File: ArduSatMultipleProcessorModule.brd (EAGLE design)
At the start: 95.5 x 90.3 mm, 82 parts, among them IC1 ATMEGA328P, IC2 ATMEGA328P, IC3 ATMEGA328P, IC4 ATMEGA328P, IC5 MCP23017SO, IC6 MCP23017SO, P1 N1_ICSP, P2 N0_ICSP, P3 N0_ICSP, P4 N1_ICSP, Q1 BSS138 N-MOSFET, Q2 BSS138 N-MOSFET, Q3 BSS138 N-MOSFET, Q4 BSS138 N-MOSFET, Q5 BSS138 N-MOSFET, Q6 BSS138 N-MOSFET, Q7 BSS138 N-MOSFET, Q8 BSS138 N-MOSFET, U1 MUX-74HC4067, U2 MUX-74HC4067

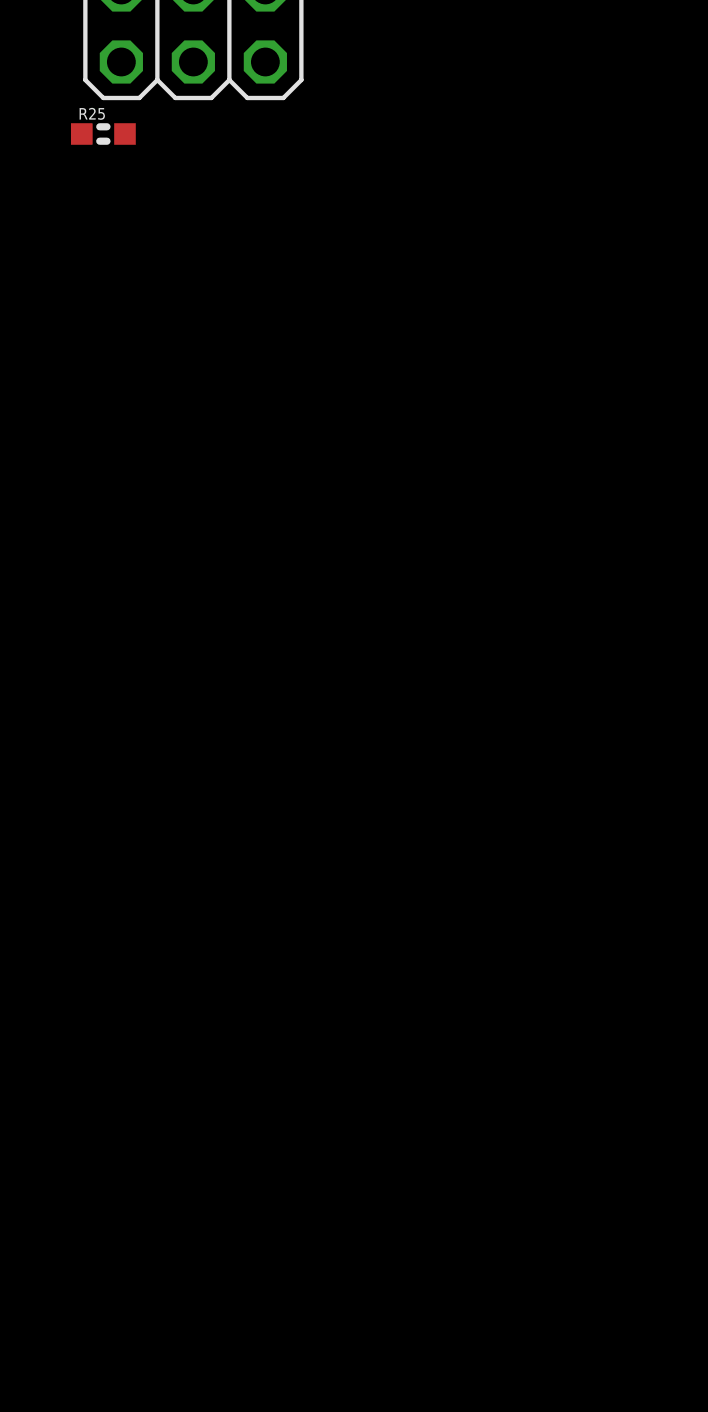
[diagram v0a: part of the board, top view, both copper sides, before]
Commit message: Testing replacement of latches using ATmega328
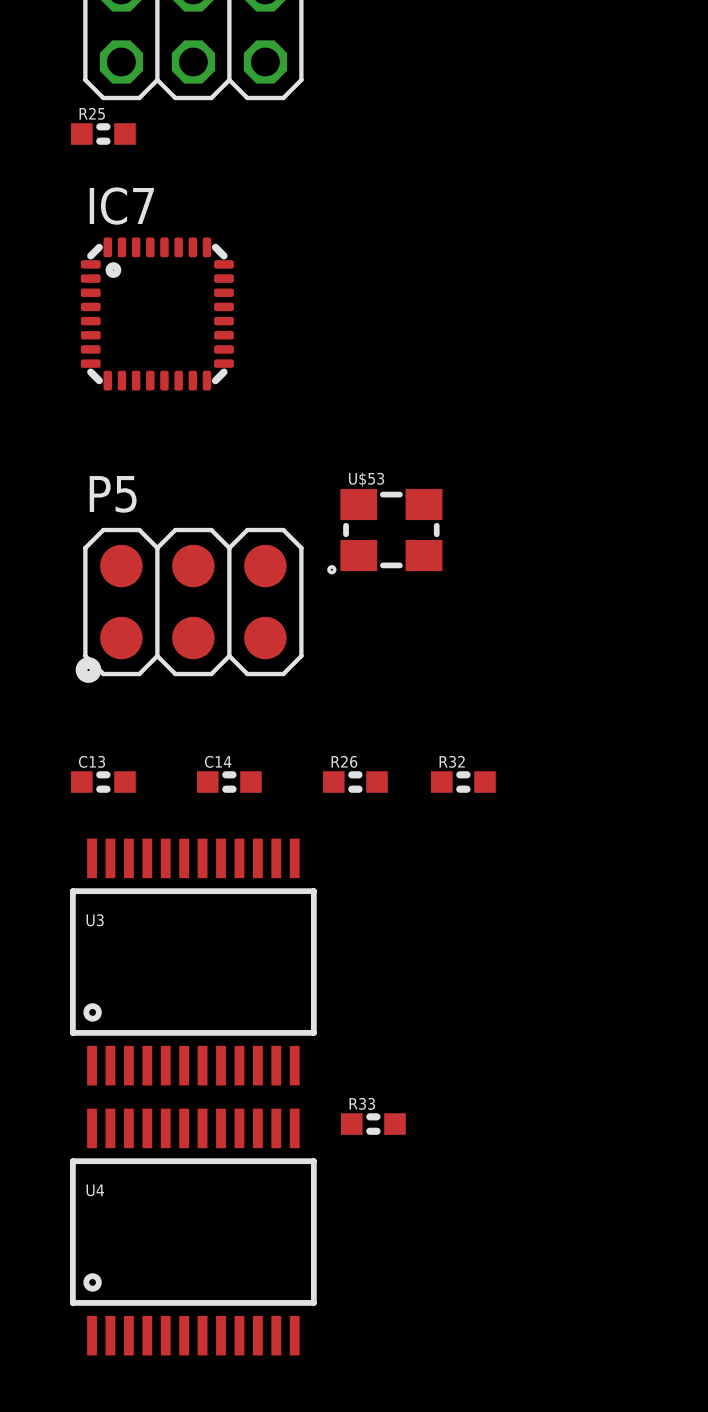
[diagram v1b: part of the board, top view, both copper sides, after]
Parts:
- added C13, C14: 22pF 0603, freetronics-master-v1.1:0603
- added IC7: ATMEGA328P, freetronics-master-v1.1:MLF32
- added P5: N1_ICSP, freetronics-jon:2X03SURFACE
- added R26: 22K 0603, freetronics-master-v1.1:0603
- added R32: 1M 0603, freetronics-master-v1.1:0603
- added R33: 33K 0603, freetronics-master-v1.1:0603
- added U$53: CRYSTAL-GND3X2, freetronics-jon:CRYSTAL-SMD-3X2
- added U3, U4: MUX-74HC4067, SparkFun:SSOP24
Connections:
- removed net MGMNT_SCL: IC5.12, IC6.12, R25.1, R27.1
- removed net MGMNT_SDA: IC5.13, IC6.13, R24.1, R28.1
- removed net S0: IC5.21, U1.10, U2.10
- removed net S1: IC5.22, U1.11, U2.11
- removed net S2: IC5.23, U1.14, U2.14
- removed net S3: IC5.24, U1.13, U2.13
- new net N$22: C14.2, IC7.8, R32.1, U$53.3
- new net N$23: C13.2, IC7.7, R32.2, U$53.1
- new net S_A0: IC5.21, IC7.23, U1.10, U2.10, U3.10, U4.10
- new net S_A1: IC5.22, IC7.24, U1.11, U2.11, U3.11, U4.11
- new net S_A2: IC5.23, IC7.25, U1.14, U2.14, U3.14, U4.14
- new net S_A3: IC5.24, IC7.26, U1.13, U2.13, U3.13, U4.13
- new net S_A4_SDA: IC5.13, IC6.13, IC7.27, R24.1, R28.1
- new net S_A5_SCL: IC5.12, IC6.12, IC7.28, R25.1, R27.1
- new net S_A6: IC7.19
- new net S_A7: IC7.22
- new net S_D0_RX: IC7.30
- new net S_D10: IC7.14
- new net S_D11_MOSI: IC7.15, P5.4
- new net S_D12_MISO: IC7.16, P5.1
- new net S_D13_SCK: IC7.17, P5.3
- new net S_D1_TX: IC7.31
- new net S_D2: IC7.32
- new net S_D3: IC7.1
- new net S_D4: IC7.2
- new net S_D5: IC7.9
- new net S_D6: IC7.10
- new net S_D7: IC7.11
- new net S_D8: IC7.12
- new net S_D9: IC7.13
- new net S_RESET: IC7.29, P5.5, R26.1
- net +5V_SYS: now also IC7.18, IC7.20, IC7.4, IC7.6, P5.2, R26.2, U3.24, U4.24
- net EN: now also R33.2, U3.15, U4.15
- net GND: now also C13.1, C14.1, IC7.21, IC7.3, IC7.5, P5.6, R33.1, U$53.2, U$53.4, U3.12, U4.12
- net N0_D0_RX: now also U4.9
- net N0_D1_TX: now also U3.9
- net N10_D0_RX: now also U4.21
- net N10_D1_TX: now also U3.21
- net N11_D0_RX: now also U4.20
- net N11_D1_TX: now also U3.20
- net N12_D0_RX: now also U4.19
- net N12_D1_TX: now also U3.19
- net N13_D0_RX: now also U4.18
- net N13_D1_TX: now also U3.18
- net N14_D0_RX: now also U4.17
- net N14_D1_TX: now also U3.17
- net N15_D0_RX: now also U4.16
- net N15_D1_TX: now also U3.16
- net N1_D0_RX: now also U4.8
- net N1_D1_TX: now also U3.8
- net N2_D0_RX: now also U4.7
- net N2_D1_TX: now also U3.7
- net N3_D0_RX: now also U4.6
- net N3_D1_TX: now also U3.6
- net N4_D0_RX: now also U4.5
- net N4_D1_TX: now also U3.5
- net N5_D0_RX: now also U4.4
- net N5_D1_TX: now also U3.4
- net N6_D0_RX: now also U4.3
- net N6_D1_TX: now also U3.3
- net N7_D0_RX: now also U4.2
- net N7_D1_TX: now also U3.2
- net N8_D0_RX: now also U4.23
- net N8_D1_TX: now also U3.23
- net N9_D0_RX: now also U4.22
- net N9_D1_TX: now also U3.22
- net RX: now also U4.1
- net TX: now also U3.1

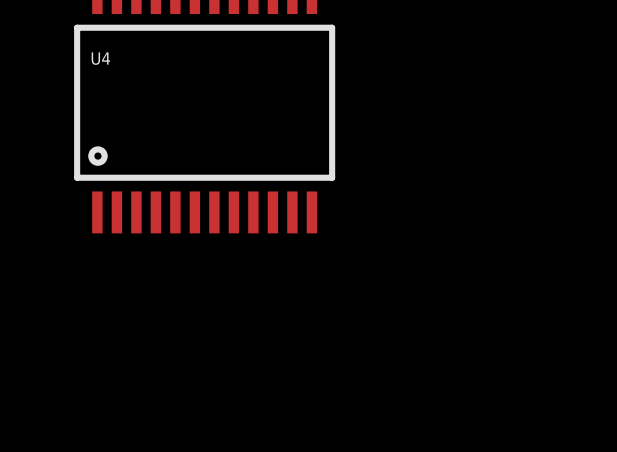
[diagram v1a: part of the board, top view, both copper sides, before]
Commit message: Added alternative supervisor node
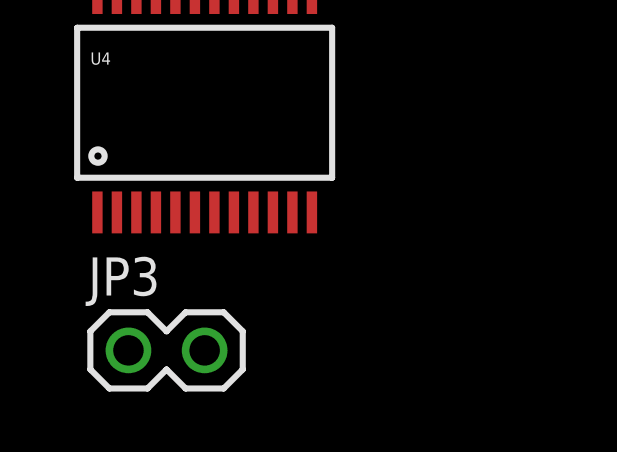
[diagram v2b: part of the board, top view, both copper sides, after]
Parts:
- added JP3: (no value), freetronics-master-v1.1:1X02
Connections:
- net RX: now also JP3.2
- net TX: now also JP3.1
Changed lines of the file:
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@@
 <element name="U4" library="SparkFun" package="SSOP24" value="MUX-74HC4067" x="1.27" y="-220.345"/>
 <element name="R33" library="freetronics-master-v1.1" package="0603" value="33K 0603" x="7.62" y="-216.535"/>
+<element name="JP3" library="freetronics-master-v1.1" package="1X02" value="" x="-1.27" y="-228.6"/>
 </elements>
 <signals>
@@
 <contactref element="U1" pad="1"/>
 <contactref element="U3" pad="1"/>
+<contactref element="JP3" pad="1"/>
+<wire x1="-2.305" y1="-214.476" x2="-1.27" y2="-228.6" width="0" layer="19" extent="1-1"/>
 <wire x1="-2.305" y1="-86.841" x2="-2.305" y2="-214.476" width="0" layer="19" extent="1-1"/>
 </signal>
@@
 <contactref element="U2" pad="1"/>
 <contactref element="U4" pad="1"/>
+<contactref element="JP3" pad="2"/>
+<wire x1="-2.305" y1="-224.001" x2="1.27" y2="-228.6" width="0" layer="19" extent="1-1"/>
 <wire x1="-2.305" y1="-109.701" x2="-2.305" y2="-224.001" width="0" layer="19" extent="1-1"/>
 </signal>

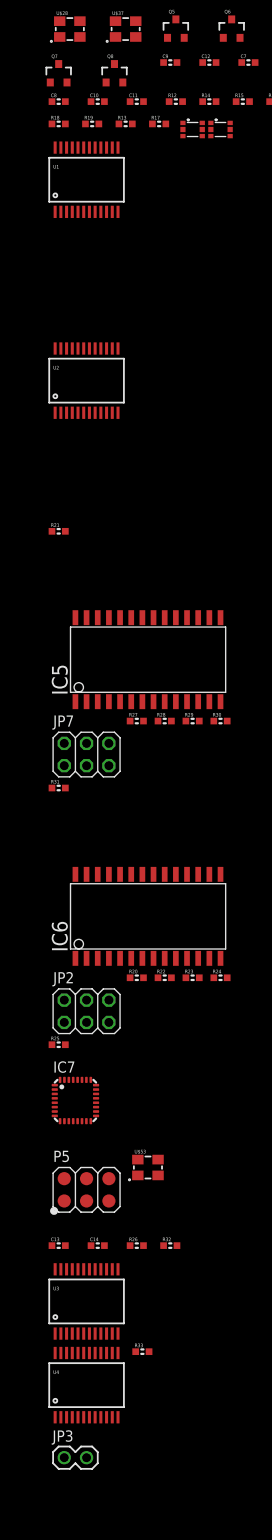
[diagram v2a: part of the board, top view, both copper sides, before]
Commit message: Added VCC control for nodes 0 and 1
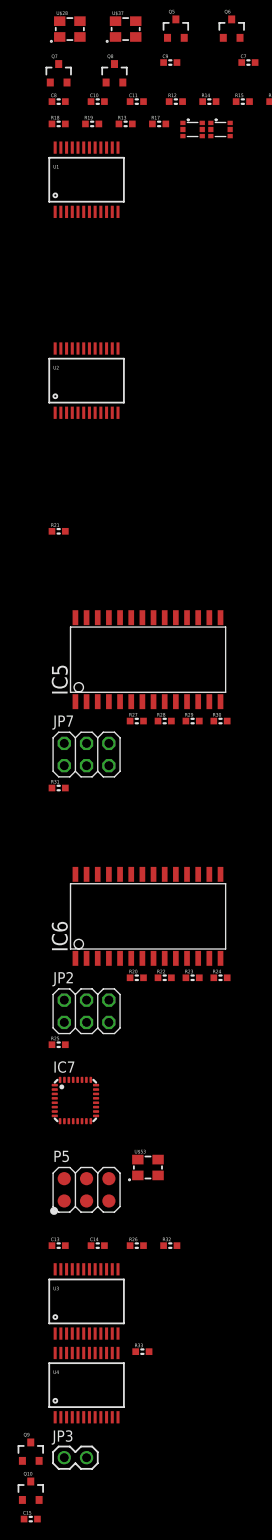
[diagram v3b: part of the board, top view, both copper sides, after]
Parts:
- removed C12: 100nF 0603, freetronics-master-v1.1:0603
- added C15: 100nF 0603, freetronics-master-v1.1:0603
- added Q10, Q9: 2N7002 N-MOSFET, freetronics-master-v1:SOT23-3
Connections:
- net EN renamed UART_EN
- net S_D0_RX renamed S_D0_N2_PWR
- net S_D1_TX renamed S_D1_N3_PWR
- net S_D2 renamed S_D2_N4_PWR
- net S_D3 renamed S_D3_N5_PWR
- net S_D4 renamed S_D4_N6_PWR
- removed net S_A6: IC7.19
- removed net S_A7: IC7.22
- new net S_A6_N0_PWR: IC7.19, Q9.1
- new net S_A7_N1_PWR: IC7.22, Q10.1
- net +5V_SYS: now also Q10.2, Q9.2
- net GND: now also C15.2; no longer C12.2
- net N0_5V: now also Q9.3
- net N1_5V: now also C15.1, Q10.3; no longer C12.1
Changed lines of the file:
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@@
 <element name="C10" library="freetronics-master-v1.1" package="0603" value="22pF 0603" x="2.54" y="-74.295"/>
 <element name="C11" library="freetronics-master-v1.1" package="0603" value="22pF 0603" x="6.985" y="-74.295"/>
-<element name="C12" library="freetronics-master-v1.1" package="0603" value="100nF 0603" x="15.24" y="-69.85"/>
 <element name="R16" library="freetronics-master-v1.1" package="0603" value="22K 0603" x="22.86" y="-74.295"/>
 <element name="P4" library="freetronics-jon" package="2X03SURFACE" value="N1_ICSP" x="10.16" y="-58.42"/>
@@
 <element name="R33" library="freetronics-master-v1.1" package="0603" value="33K 0603" x="7.62" y="-216.535"/>
 <element name="JP3" library="freetronics-master-v1.1" package="1X02" value="" x="-1.27" y="-228.6"/>
+<element name="Q9" library="freetronics-master-v1" package="SOT23-3" value="2N7002 N-MOSFET" x="-5.08" y="-227.965"/>
+<element name="C15" library="freetronics-master-v1.1" package="0603" value="100nF 0603" x="-5.08" y="-235.585"/>
+<element name="Q10" library="freetronics-master-v1" package="SOT23-3" value="2N7002 N-MOSFET" x="-5.08" y="-232.41"/>
 </elements>
 <signals>
@@
 <contactref element="U$37" pad="2"/>
 <contactref element="U$37" pad="4"/>
-<contactref element="C12" pad="2"/>
 <contactref element="IC4" pad="21"/>
 <contactref element="IC4" pad="3"/>
@@
 <contactref element="U3" pad="12"/>
 <contactref element="U4" pad="12"/>
+<contactref element="C15" pad="2"/>
+<wire x1="4.845" y1="-224.001" x2="-4.318" y2="-235.585" width="0" layer="19" extent="1-1"/>
 <wire x1="6.858" y1="-216.535" x2="4.845" y2="-224.001" width="0" layer="19" extent="1-1"/>
 <wire x1="4.845" y1="-214.476" x2="6.858" y2="-216.535" width="0" layer="19" extent="1-1"/>
@@
 <wire x1="-2.667" y1="-74.295" x2="1.778" y2="-74.295" width="0" layer="19" extent="1-1"/>
 <wire x1="11.557" y1="-69.85" x2="6.223" y2="-74.295" width="0" layer="19" extent="1-1"/>
-<wire x1="16.002" y1="-69.85" x2="11.557" y2="-69.85" width="0" layer="19" extent="1-1"/>
-<wire x1="18.923" y1="-69.85" x2="16.002" y2="-69.85" width="0" layer="19" extent="1-1"/>
 <wire x1="6.865" y1="-66.94" x2="11.557" y2="-69.85" width="0" layer="19" extent="1-1"/>
 <wire x1="4.565" y1="-65.14" x2="6.865" y2="-66.94" width="0" layer="19" extent="1-1"/>
 <wire x1="0.515" y1="-66.94" x2="4.565" y2="-65.14" width="0" layer="19" extent="1-1"/>
 <wire x1="-1.785" y1="-65.14" x2="0.515" y2="-66.94" width="0" layer="19" extent="1-1"/>
+<wire x1="18.923" y1="-69.85" x2="11.557" y2="-69.85" width="0" layer="19" extent="1-1"/>
 <wire x1="3.81" y1="-57.15" x2="4.565" y2="-65.14" width="0" layer="19" extent="1-1"/>
 <wire x1="12.7" y1="-57.15" x2="3.81" y2="-57.15" width="0" layer="19" extent="1-1"/>
@@
 <contactref element="IC7" pad="20"/>
 <contactref element="R26" pad="2"/>
+<contactref element="Q9" pad="2"/>
+<contactref element="Q10" pad="2"/>
+<wire x1="-4.13" y1="-228.965" x2="-4.13" y2="-233.41" width="0" layer="19" extent="1-1"/>
+<wire x1="-2.305" y1="-216.689" x2="-4.13" y2="-228.965" width="0" layer="19" extent="1-1"/>
 <wire x1="-2.305" y1="-207.164" x2="-2.305" y2="-216.689" width="0" layer="19" extent="1-1"/>
 <wire x1="-1.27" y1="-196.85" x2="-2.305" y2="-207.164" width="0" layer="19" extent="1-1"/>
@@
 <contactref element="R15" pad="2"/>
 <contactref element="IC6" pad="21"/>
+<contactref element="Q9" pad="3"/>
+<wire x1="8.89" y1="-162.225" x2="-5.08" y2="-226.865" width="0" layer="19" extent="1-1"/>
 <wire x1="14.435" y1="-78.22" x2="8.89" y2="-162.225" width="0" layer="19" extent="1-1"/>
 <wire x1="14.435" y1="-77.47" x2="14.435" y2="-78.22" width="0" layer="19" extent="1-1"/>
@@
 <contactref element="Q7" pad="1"/>
 <contactref element="R18" pad="2"/>
-<contactref element="C12" pad="1"/>
 <contactref element="R16" pad="2"/>
 <contactref element="P4" pad="2"/>
@@
 <contactref element="IC4" pad="20"/>
 <contactref element="IC6" pad="22"/>
+<contactref element="C15" pad="1"/>
+<contactref element="Q10" pad="3"/>
+<wire x1="-5.08" y1="-231.31" x2="-5.842" y2="-235.585" width="0" layer="19" extent="1-1"/>
+<wire x1="7.62" y1="-162.225" x2="-5.08" y2="-231.31" width="0" layer="19" extent="1-1"/>
 <wire x1="17.61" y1="-78.22" x2="7.62" y2="-162.225" width="0" layer="19" extent="1-1"/>
 <wire x1="17.61" y1="-77.47" x2="17.61" y2="-78.22" width="0" layer="19" extent="1-1"/>
 <wire x1="23.622" y1="-74.295" x2="17.61" y2="-77.47" width="0" layer="19" extent="1-1"/>
-<wire x1="14.478" y1="-69.85" x2="17.61" y2="-77.47" width="0" layer="19" extent="1-1"/>
-<wire x1="3.495" y1="-72.12" x2="14.478" y2="-69.85" width="0" layer="19" extent="1-1"/>
-<wire x1="2.667" y1="-76.835" x2="3.495" y2="-72.12" width="0" layer="19" extent="1-1"/>
+<wire x1="2.667" y1="-76.835" x2="17.61" y2="-77.47" width="0" layer="19" extent="1-1"/>
 <wire x1="-1.143" y1="-76.835" x2="2.667" y2="-76.835" width="0" layer="19" extent="1-1"/>
+<wire x1="3.495" y1="-72.12" x2="2.667" y2="-76.835" width="0" layer="19" extent="1-1"/>
 <wire x1="-2.855" y1="-72.12" x2="-1.143" y2="-76.835" width="0" layer="19" extent="1-1"/>
-<wire x1="7.62" y1="-57.15" x2="14.478" y2="-69.85" width="0" layer="19" extent="1-1"/>
+<wire x1="7.62" y1="-57.15" x2="3.495" y2="-72.12" width="0" layer="19" extent="1-1"/>
 <wire x1="10.35" y1="-49.01" x2="7.62" y2="-57.15" width="0" layer="19" extent="1-1"/>
 <wire x1="10.35" y1="-48.01" x2="10.35" y2="-49.01" width="0" layer="19" extent="1-1"/>
@@
 <wire x1="1.25" y1="-20.13" x2="1.27" y2="-26.67" width="0" layer="19" extent="1-1"/>
 </signal>
-<signal name="EN">
+<signal name="UART_EN">
 <contactref element="U1" pad="15"/>
 <contactref element="U2" pad="15"/>
@@
 <contactref element="IC6" pad="8"/>
 </signal>
-<signal name="S_A6">
+<signal name="S_A6_N0_PWR">
 <contactref element="IC7" pad="19"/>
-</signal>
-<signal name="S_A7">
-<contactref element="IC7" pad="22"/>
-</signal>
-<signal name="S_D2">
+<contactref element="Q9" pad="1"/>
+<wire x1="2.35" y1="-188.71" x2="-6.03" y2="-228.965" width="0" layer="19" extent="1-1"/>
+</signal>
+<signal name="S_D2_N4_PWR">
 <contactref element="IC7" pad="32"/>
 </signal>
-<signal name="S_D3">
+<signal name="S_D3_N5_PWR">
 <contactref element="IC7" pad="1"/>
 </signal>
-<signal name="S_D4">
+<signal name="S_D4_N6_PWR">
 <contactref element="IC7" pad="2"/>
 </signal>
@@
 <contactref element="IC7" pad="14"/>
 </signal>
-<signal name="S_D0_RX">
+<signal name="S_D0_N2_PWR">
 <contactref element="IC7" pad="30"/>
 </signal>
-<signal name="S_D1_TX">
+<signal name="S_D1_N3_PWR">
 <contactref element="IC7" pad="31"/>
 </signal>
@@
 <wire x1="-0.25" y1="-185.61" x2="3.81" y2="-199.39" width="0" layer="19" extent="1-1"/>
 </signal>
+<signal name="S_A7_N1_PWR">
+<contactref element="Q10" pad="1"/>
+<contactref element="IC7" pad="22"/>
+<wire x1="2.35" y1="-187.21" x2="-6.03" y2="-233.41" width="0" layer="19" extent="1-1"/>
+</signal>
 </signals>
